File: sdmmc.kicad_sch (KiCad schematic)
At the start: 4 parts, among them J4 MSD-4-A

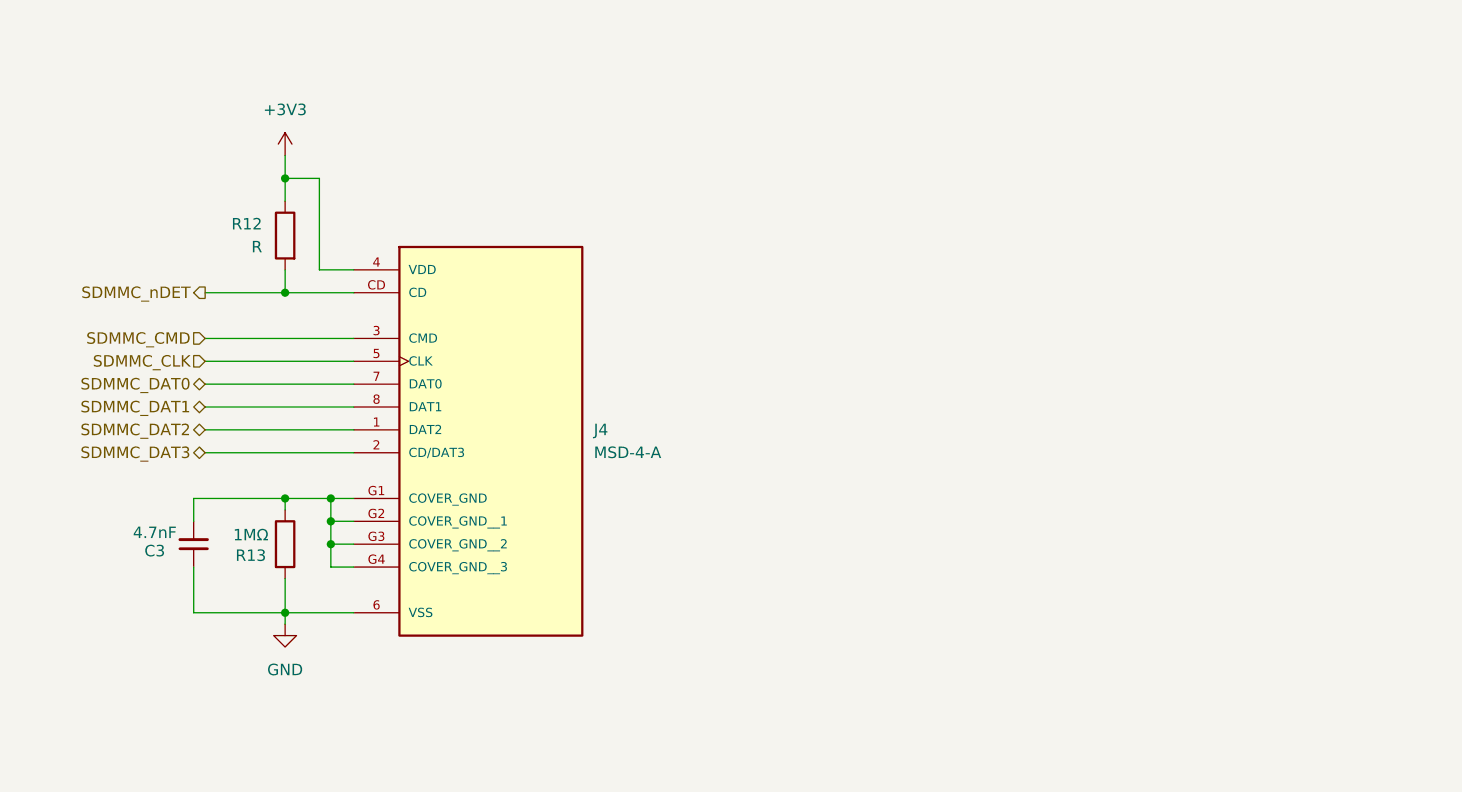
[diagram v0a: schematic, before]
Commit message: Added pull-ups to sdmmc
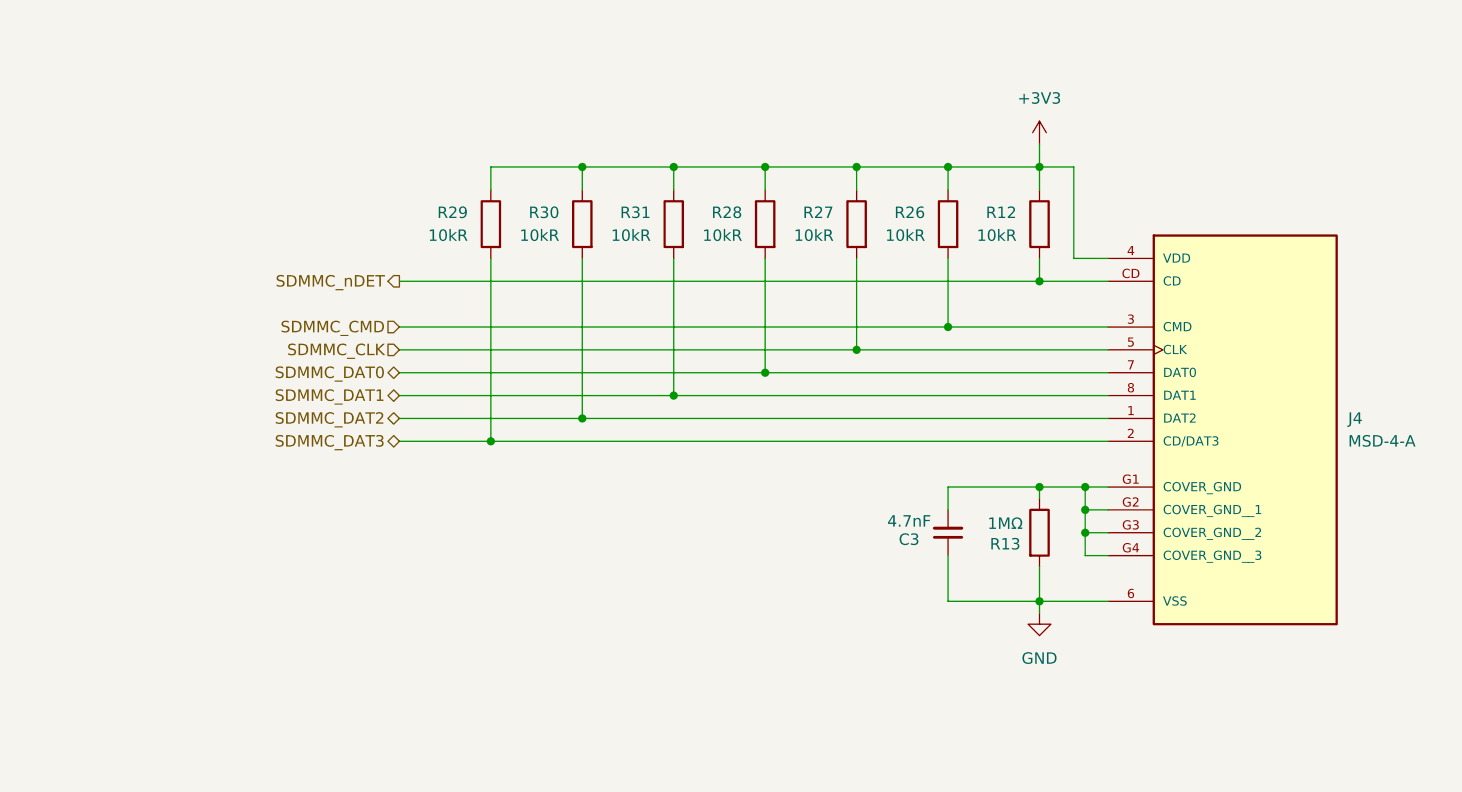
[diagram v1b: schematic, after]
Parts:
- added R26, R27, R28, R29, R30, R31: 10kR, Resistor_SMD:R_0805_2012Metric_Pad1.20x1.40mm_HandSolder, symbol Device:R
- R12: value R -> 10kR
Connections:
- net +3V3: now also R26.1, R27.1, R28.1, R29.1, R30.1, R31.1
- net SDMMC_CLK: now also R27.2
- net SDMMC_CMD: now also R26.2
- net SDMMC_DAT0: now also R28.2
- net SDMMC_DAT1: now also R31.2
- net SDMMC_DAT2: now also R30.2
- net SDMMC_DAT3: now also R29.2
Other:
- moved on the sheet: C3, J4, R12, R13

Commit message: Added MCU power connections
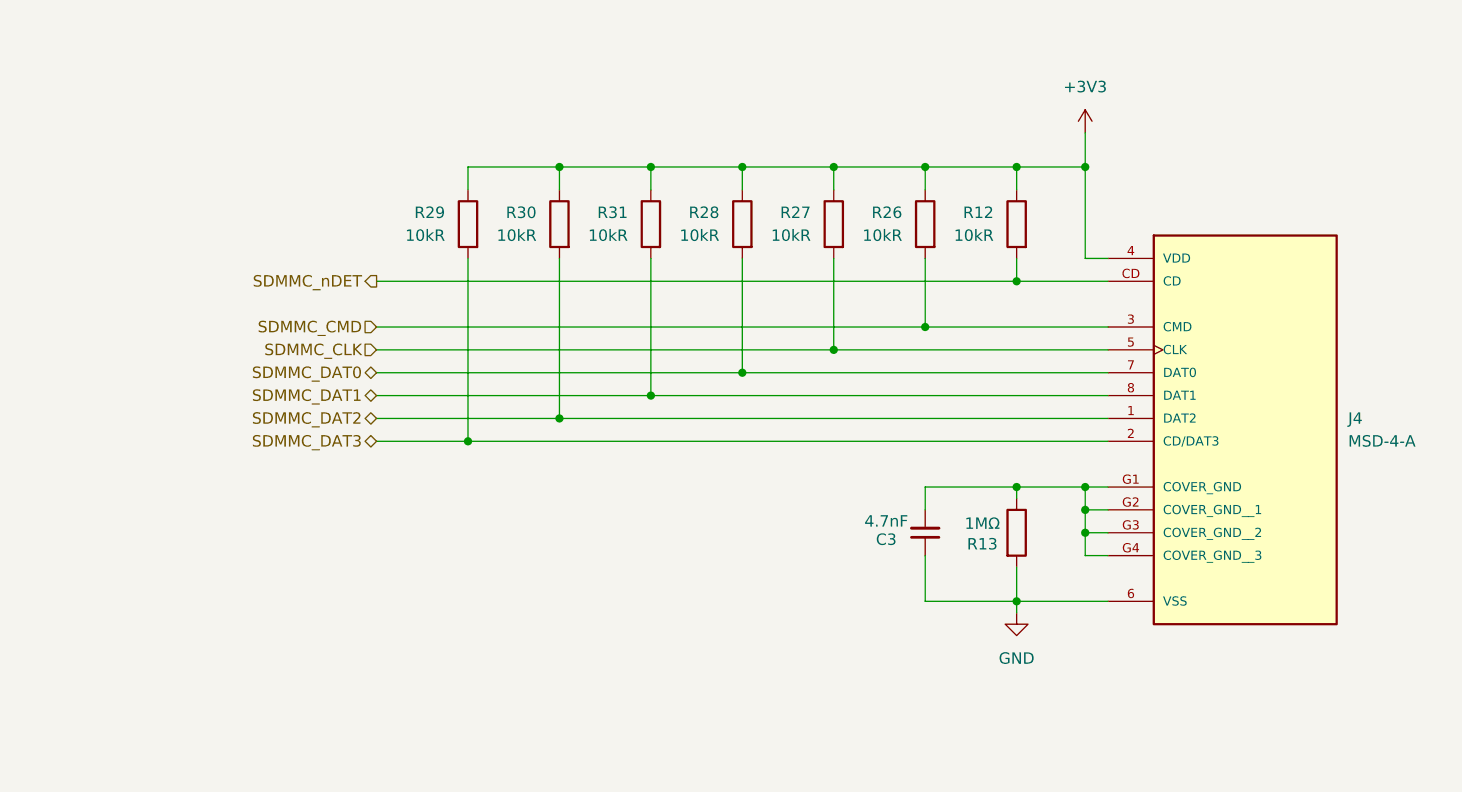
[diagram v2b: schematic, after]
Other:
- moved on the sheet: C3, R12, R13, R26, R27, R28, R29, R30, R31

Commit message: layout v1
no silkscreen done yet
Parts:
- added C24: 100nF, Capacitor_SMD:C_0805_2012Metric_Pad1.18x1.45mm_HandSolder, symbol Device:C_Small
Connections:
- net +3V3: now also C24.1
- net GND: now also C24.2
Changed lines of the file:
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@@
+	)
+	(junction
+		(at 153.67 22.86)
+		(diameter 0)
+		(color 255 0 0 1)
 	)
 	(junction
@@
 	(wire
 		(pts
+			(xy 153.67 22.86) (xy 153.67 30.48)
+		)
+		(stroke
+			(width 0.3048)
+			(type default)
+			(color 255 0 0 1)
+		)
+	)
+	(wire
+		(pts
 			(xy 146.05 30.48) (xy 146.05 33.02)
 		)
@@
 	(wire
 		(pts
-			(xy 153.67 26.67) (xy 153.67 30.48)
+			(xy 153.67 20.32) (xy 153.67 22.86)
 		)
 		(stroke
@@
 	(wire
 		(pts
+			(xy 160.02 29.21) (xy 160.02 30.48)
+		)
+		(stroke
+			(width 0.3048)
+			(type default)
+			(color 0 0 0 1)
+		)
+	)
+	(wire
+		(pts
 			(xy 95.25 30.48) (xy 105.41 30.48)
 		)
@@
 			(width 0)
 			(type default)
+		)
+	)
+	(wire
+		(pts
+			(xy 160.02 24.13) (xy 160.02 22.86)
+		)
+		(stroke
+			(width 0.3048)
+			(type default)
+			(color 255 0 0 1)
+		)
+	)
+	(wire
+		(pts
+			(xy 160.02 22.86) (xy 153.67 22.86)
+		)
+		(stroke
+			(width 0.3048)
+			(type default)
+			(color 255 0 0 1)
 		)
 	)
@@
 				(path "/2f7e2d6e-7ac1-4ae5-be0e-a6d141d8b943/5ffa423e-bf19-4bb0-947b-4e60d995962a"
 					(reference "R29")
+					(unit 1)
+				)
+			)
+		)
+	)
+	(symbol
+		(lib_id "power:GND")
+		(at 160.02 30.48 0)
+		(mirror y)
+		(unit 1)
+		(exclude_from_sim no)
+		(in_bom yes)
+		(on_board yes)
+		(dnp no)
+		(property "Reference" "#PWR034"
+			(at 160.02 36.83 0)
+			(effects
+				(font
+					(size 1.27 1.27)
+				)
+				(hide yes)
+			)
+		)
+		(property "Value" "GND"
+			(at 160.02 34.544 0)
+			(effects
+				(font
+					(size 1.27 1.27)
+				)
+			)
+		)
+		(property "Footprint" ""
+			(at 160.02 30.48 0)
+			(effects
+				(font
+					(size 1.27 1.27)
+				)
+				(hide yes)
+			)
+		)
+		(property "Datasheet" ""
+			(at 160.02 30.48 0)
+			(effects
+				(font
+					(size 1.27 1.27)
+				)
+				(hide yes)
+			)
+		)
+		(property "Description" "Power symbol creates a global label with name \"GND\" , ground"
+			(at 160.02 30.48 0)
+			(effects
+				(font
+					(size 1.27 1.27)
+				)
+				(hide yes)
+			)
+		)
+		(pin "1"
+		)
+		(instances
+			(project "miniServer"
+				(path "/2f7e2d6e-7ac1-4ae5-be0e-a6d141d8b943/5ffa423e-bf19-4bb0-947b-4e60d995962a"
+					(reference "#PWR034")
 					(unit 1)
 				)
@@
 	)
 	(symbol
+		(lib_id "Device:C_Small")
+		(at 160.02 26.67 0)
+		(mirror y)
+		(unit 1)
+		(exclude_from_sim no)
+		(in_bom yes)
+		(on_board yes)
+		(dnp no)
+		(property "Reference" "C24"
+			(at 162.814 28.702 90)
+			(effects
+				(font
+					(size 1.27 1.27)
+				)
+				(justify left)
+			)
+		)
+		(property "Value" "100nF"
+			(at 164.592 29.718 90)
+			(effects
+				(font
+					(size 1.27 1.27)
+				)
+				(justify left)
+			)
+		)
+		(property "Footprint" "Capacitor_SMD:C_0805_2012Metric_Pad1.18x1.45mm_HandSolder"
+			(at 160.02 26.67 0)
+			(effects
+				(font
+					(size 1.27 1.27)
+				)
+				(hide yes)
+			)
+		)
+		(property "Datasheet" "~"
+			(at 160.02 26.67 0)
+			(effects
+				(font
+					(size 1.27 1.27)
+				)
+				(hide yes)
+			)
+		)
+		(property "Description" "Unpolarized capacitor, small symbol"
+			(at 160.02 26.67 0)
+			(effects
+				(font
+					(size 1.27 1.27)
+				)
+				(hide yes)
+			)
+		)
+		(pin "2"
+		)
+		(pin "1"
+		)
+		(instances
+			(project "miniServer"
+				(path "/2f7e2d6e-7ac1-4ae5-be0e-a6d141d8b943/5ffa423e-bf19-4bb0-947b-4e60d995962a"
+					(reference "C24")
+					(unit 1)
+				)
+			)
+		)
+	)
+	(symbol
 		(lib_id "Device:R")
 		(at 146.05 71.12 0)
@@
 	(symbol
 		(lib_id "power:+3V3")
-		(at 153.67 26.67 0)
+		(at 153.67 20.32 0)
 		(unit 1)
 		(exclude_from_sim no)
@@
 		(fields_autoplaced yes)
 		(property "Reference" "#PWR016"
-			(at 153.67 30.48 0)
+			(at 153.67 24.13 0)
 			(effects
 				(font
@@
 		)
 		(property "Value" "+3V3"
-			(at 153.67 21.59 0)
+			(at 153.67 15.24 0)
 			(effects
 				(font
@@
 		)
 		(property "Footprint" ""
-			(at 153.67 26.67 0)
+			(at 153.67 20.32 0)
 			(effects
 				(font
@@
 		)
 		(property "Datasheet" ""
-			(at 153.67 26.67 0)
+			(at 153.67 20.32 0)
 			(effects
 				(font
@@
 		)
 		(property "Description" "Power symbol creates a global label with name \"+3V3\""
-			(at 153.67 26.67 0)
-			(effects
-				(font
+			(at 153.67 20.32 0)
+			(effects
+				(font

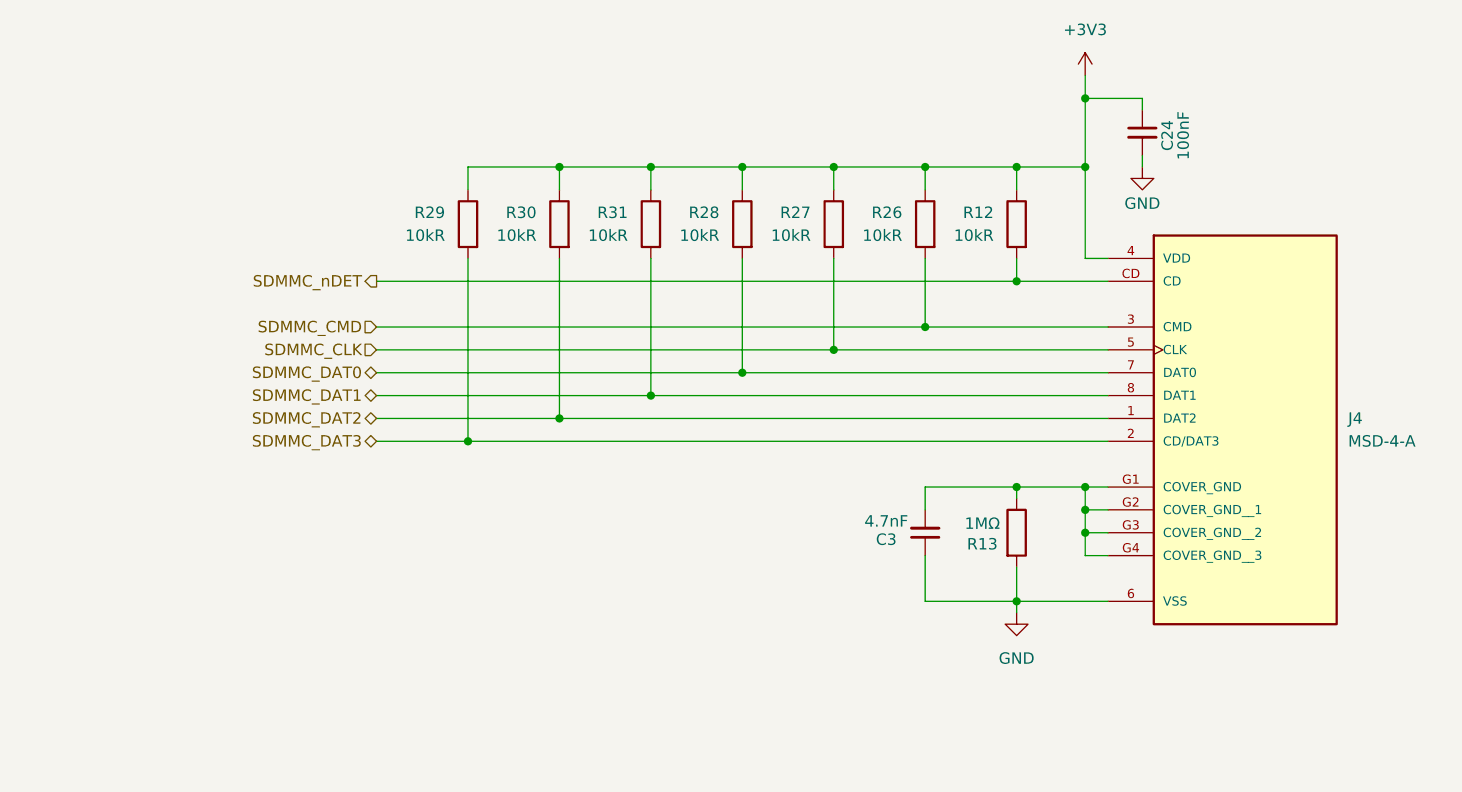
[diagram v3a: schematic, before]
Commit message: Changed comment on VCAPs of MCU + added pdf link for our configuration
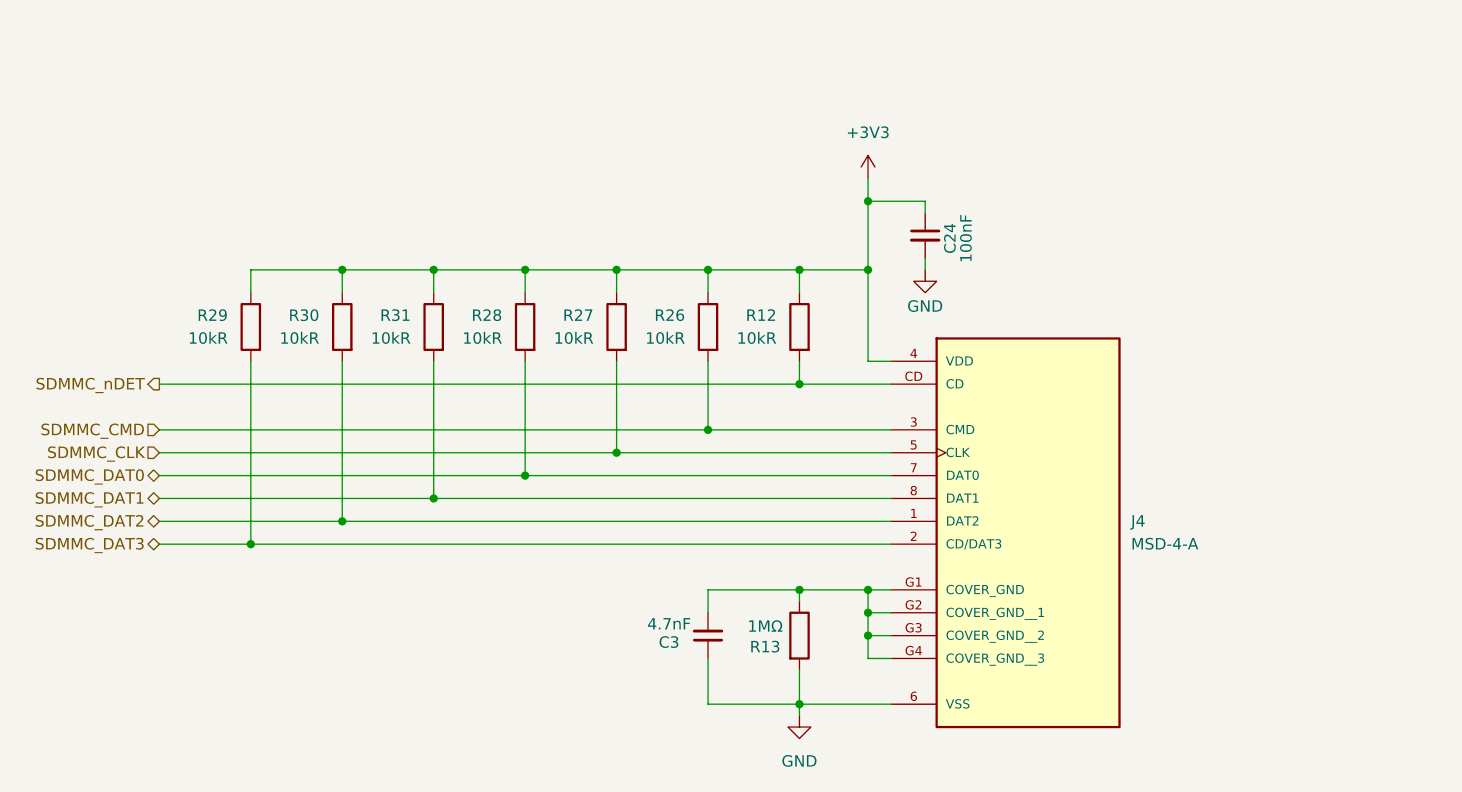
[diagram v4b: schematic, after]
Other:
- moved on the sheet: C24, C3, J4, R12, R13, R26, R27, R28, R29, R30, R31
